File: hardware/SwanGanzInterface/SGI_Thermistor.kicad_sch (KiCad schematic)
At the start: 13 parts, among them U1 INA122D, U2 OPA2350

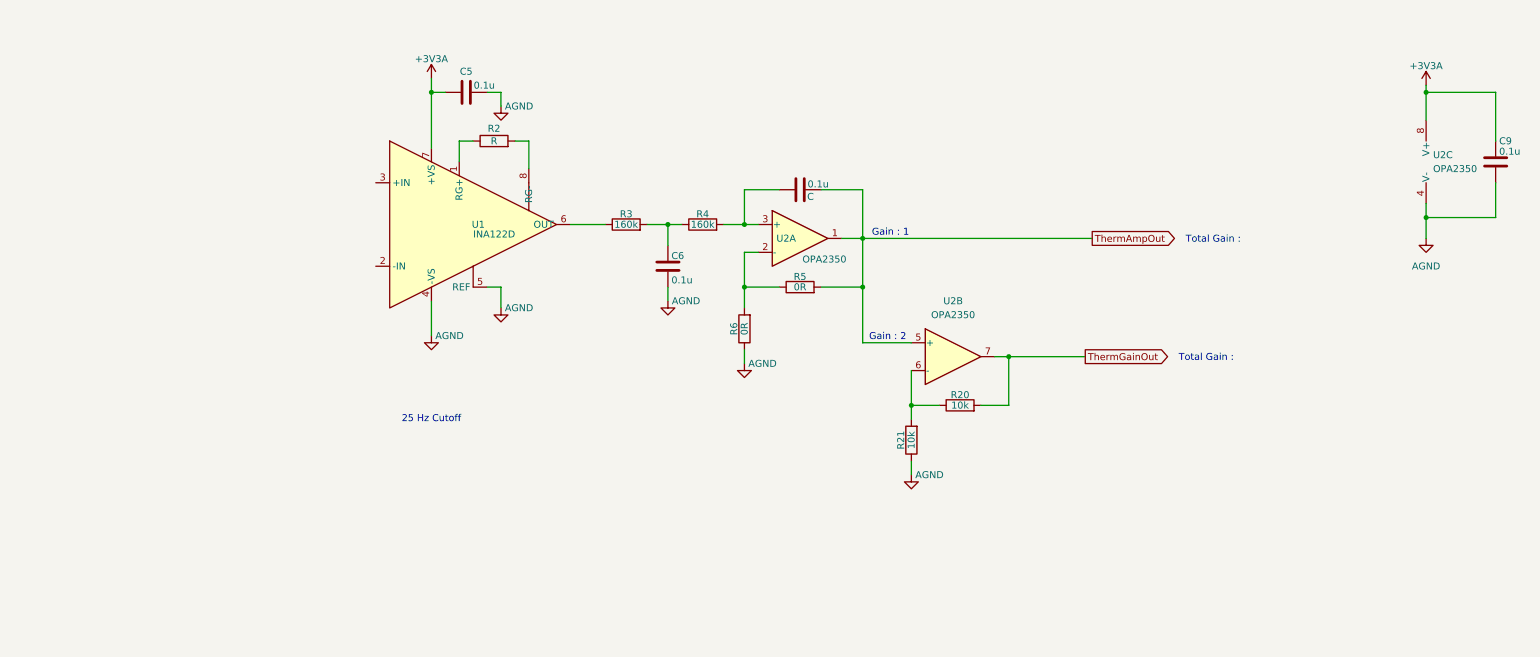
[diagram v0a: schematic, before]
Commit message: Updated gain and added power connector
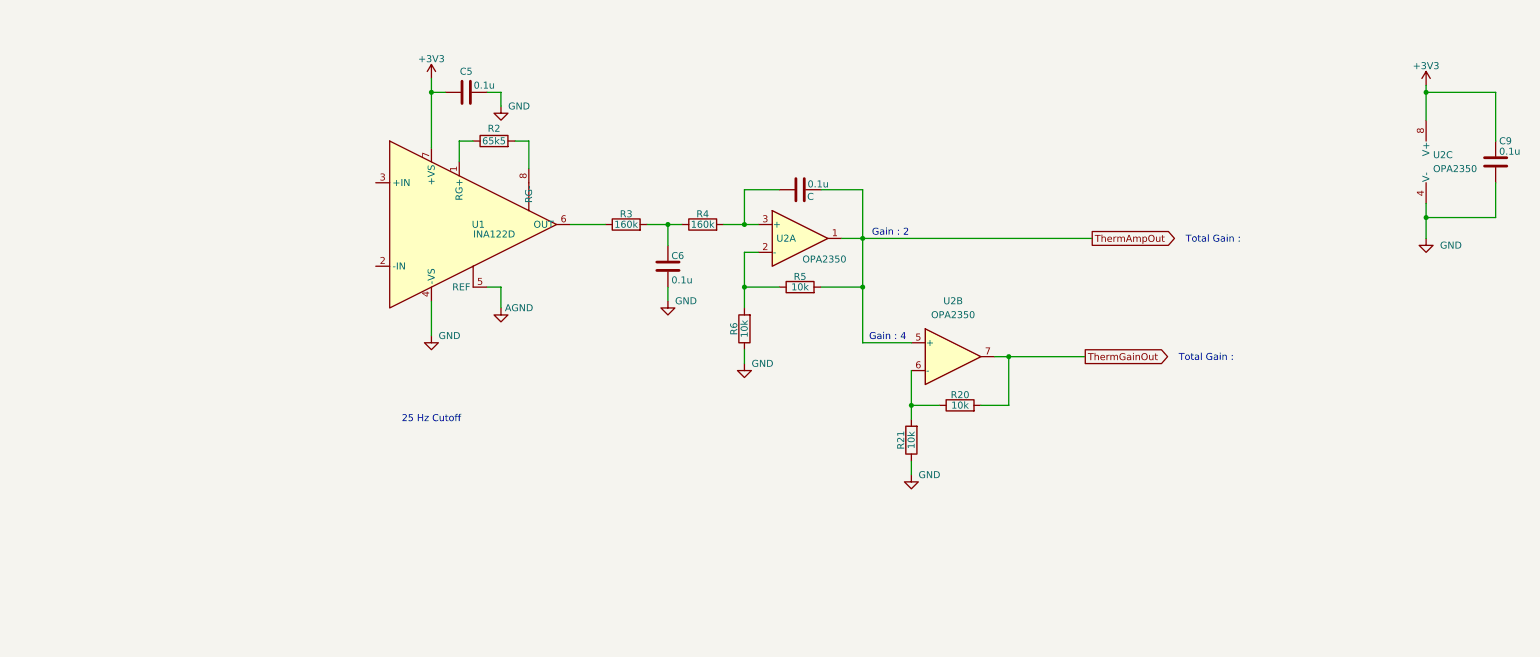
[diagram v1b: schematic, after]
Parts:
- R2: value R -> 65k5
- R5, R6: value 0R -> 10k
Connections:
- net AGND: no longer C5.1, C6.2, C9.2, R21.1, R6.1, U1.4 (-VS), U2.4 (V-)
- net +3V3A renamed +3V3
- new net GND: C5.1, C6.2, C9.2, R21.1, R6.1, U1.4 (-VS), U2.4 (V-)
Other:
- note added: "Gain : 4"
- note removed: "Gain : 1"
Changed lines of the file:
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@@
 		(comment 3 "Faculty Mentor - Dr. Valvano")
 	)
-	(text "Gain : 2"
+	(text "Gain : 4"
 		(exclude_from_sim no)
 		(at 167.132 71.374 0)
@@
 		)
 	)
-	(text "Gain : 1"
+	(text "Gain : 2\n"
 		(exclude_from_sim no)
 		(at 167.64 52.324 0)
@@
 			)
 		)
-		(property "Value" "AGND"
+		(property "Value" "GND"
 			(at 144.272 76.2 0)
 			(effects
@@
 			)
 		)
-		(property "Value" "AGND"
+		(property "Value" "GND"
 			(at 99.822 29.21 0)
 			(effects
@@
 			)
 		)
-		(property "Value" "+3V3A"
+		(property "Value" "+3V3"
 			(at 83.82 20.574 0)
 			(effects
@@
 			)
 		)
-		(property "Value" "AGND"
+		(property "Value" "GND"
 			(at 174.752 96.52 0)
 			(effects
@@
 			)
 		)
-		(property "Value" "0R"
+		(property "Value" "10k"
 			(at 140.97 69.85 90)
 			(effects
@@
 			)
 		)
-		(property "Value" "0R"
+		(property "Value" "10k"
 			(at 151.13 62.23 90)
 			(effects
@@
 			)
 		)
-		(property "Value" "AGND"
-			(at 265.43 58.42 0)
-			(effects
-				(font
-					(size 1.27 1.27)
-				)
+		(property "Value" "GND"
+			(at 267.97 54.6099 0)
+			(effects
+				(font
+					(size 1.27 1.27)
+				)
+				(justify left)
 			)
 		)
@@
 			)
 		)
-		(property "Value" "+3V3A"
+		(property "Value" "+3V3"
 			(at 265.43 21.844 0)
 			(effects
@@
 			)
 		)
-		(property "Value" "R"
+		(property "Value" "65k5"
 			(at 95.25 35.56 90)
 			(effects
@@
 			)
 		)
-		(property "Value" "AGND"
+		(property "Value" "GND"
 			(at 87.122 71.12 0)
 			(effects
@@
 			)
 		)
-		(property "Value" "AGND"
+		(property "Value" "GND"
 			(at 130.302 64.77 0)
 			(effects

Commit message: Reverse Polarity Fet, Updated Notes, Added second gain stage for pressure, General Updates
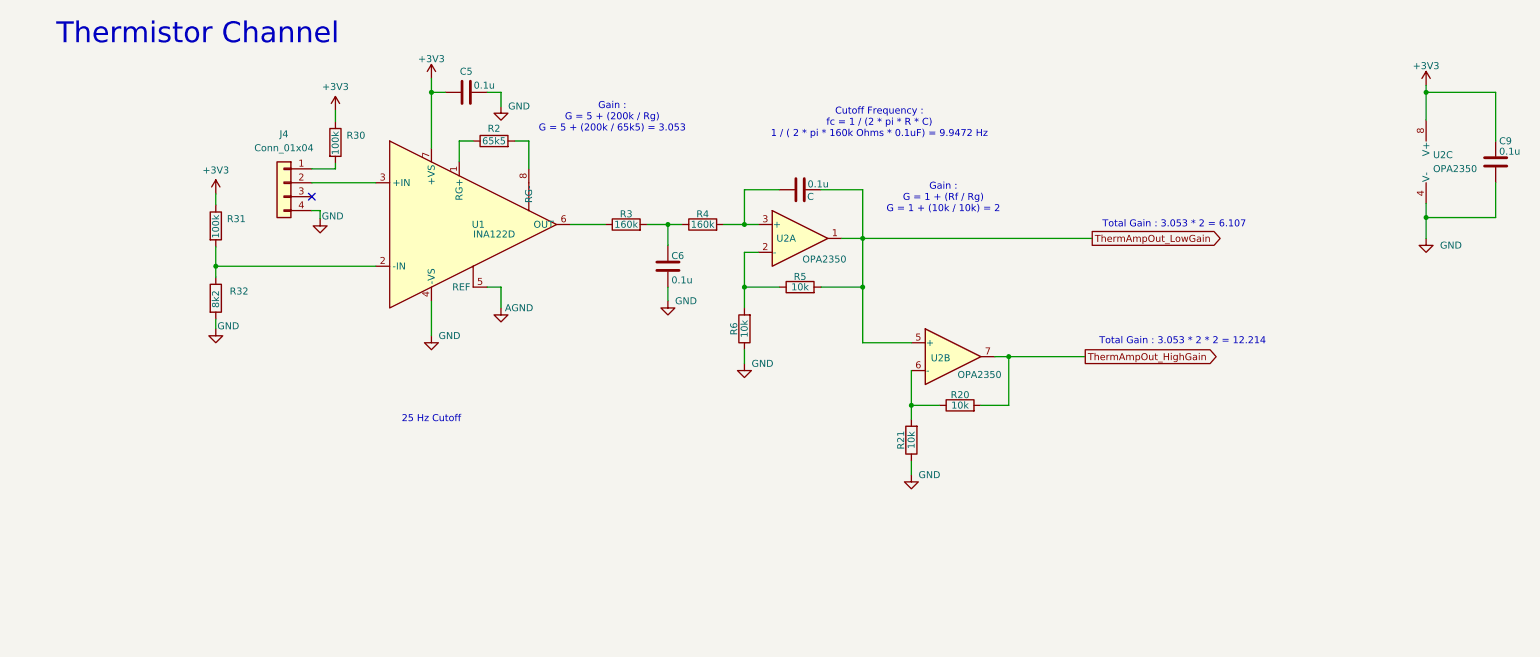
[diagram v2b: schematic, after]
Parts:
- added J4: Conn_01x04, symbol Connector_Generic:Conn_01x04
- added R30, R31: 100k, symbol Device:R
- added R32: 8k2, symbol Device:R
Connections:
- net +3V3: now also R30.1, R31.1
- net GND: now also J4.4 (Pin_4), R32.2
- net at U1.2 (-IN): now also R31.2, R32.1
- net at U1.3 (+IN): now also J4.2 (Pin_2)
- net ThermAmpOut renamed ThermAmpOut_LowGain
- net ThermGainOut renamed ThermAmpOut_HighGain
- new net: J4.1 (Pin_1), R30.2
- no-connect marks 0 -> 1
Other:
- note added: "Cutoff Frequency : fc = 1 / (2 * pi * R * C) 1 / ( 2 * pi * 160k Ohms * 0.1uF) = 9.9472 Hz"
- note added: "Gain : G = 1 + (Rf / Rg) G = 1 + (10k / 10k) = 2"
- note added: "Gain : G = 5 + (200k / Rg) G = 5 + (200k / 65k5) = 3.053"
- note added: "Thermistor Channel"
- note added: "Total Gain : 3.053 * 2 * 2 = 12.214"
- note added: "Total Gain : 3.053 * 2 = 6.107"
- note removed: "Gain : 2"
- note removed: "Gain : 4"
- note removed: "Total Gain :"

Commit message: Added launchpad, power jumpers, messed with symbol lib
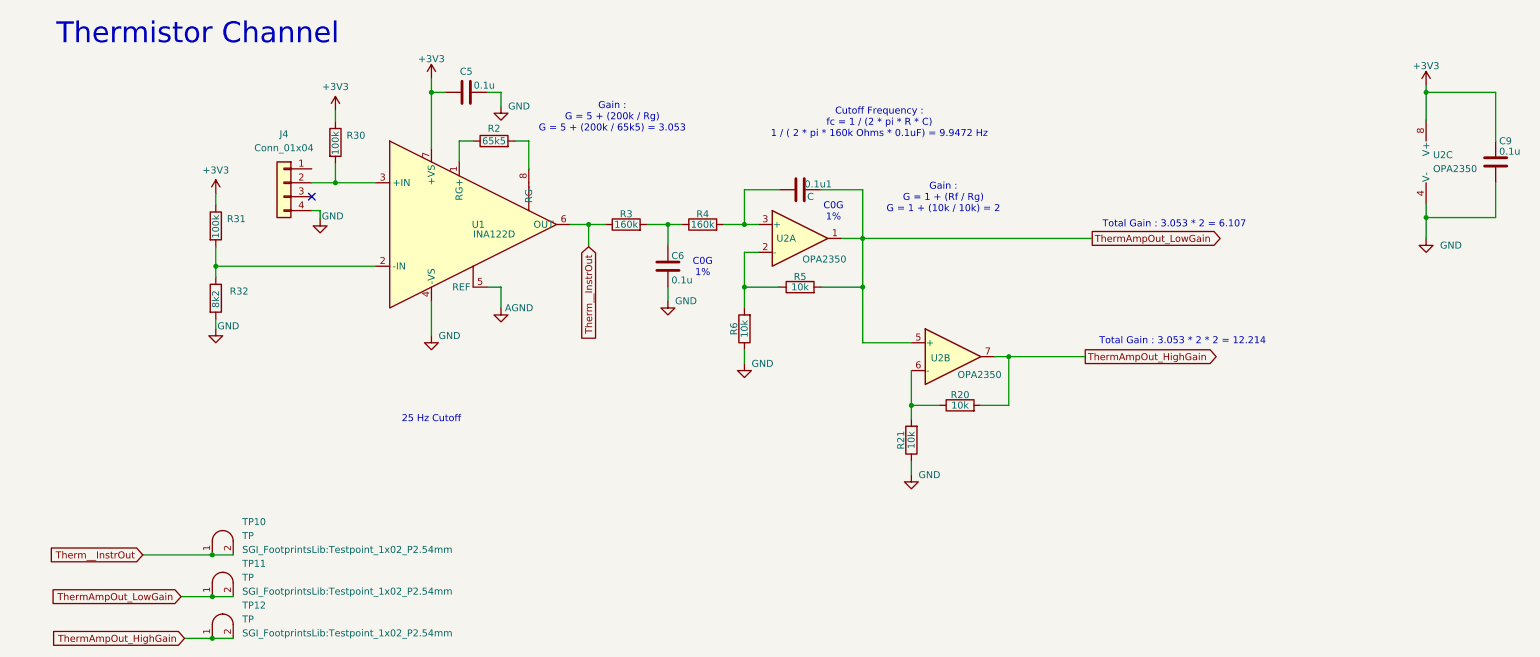
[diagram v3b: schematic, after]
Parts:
- added TP10, TP11, TP12: TP, SGI_FootprintsLib:Testpoint_1x02_P2.54mm, symbol SGI_SymbolLib:Testpoint
- renumbered 0.1u to 0.1u1
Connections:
- net ThermAmpOut_HighGain: now also TP12.1 (A), TP12.2 (B)
- net ThermAmpOut_LowGain: now also TP11.1 (A), TP11.2 (B)
- net at R30.2: now also J4.2 (Pin_2), U1.3 (+IN); no longer J4.1 (Pin_1)
- net Therm__InstrOut: now reaches R3.1, U1.6 (OUT)
- net Therm__InstrOut: now also TP10.1 (A), TP10.2 (B)
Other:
- note added: "C0G 1%"
